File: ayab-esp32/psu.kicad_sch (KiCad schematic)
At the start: 48 parts, among them J602 940, J603 910.930.950.CK35, Q601 BCM857BV, Q602 AO3401A, U401 XL1509, U402 XL1509

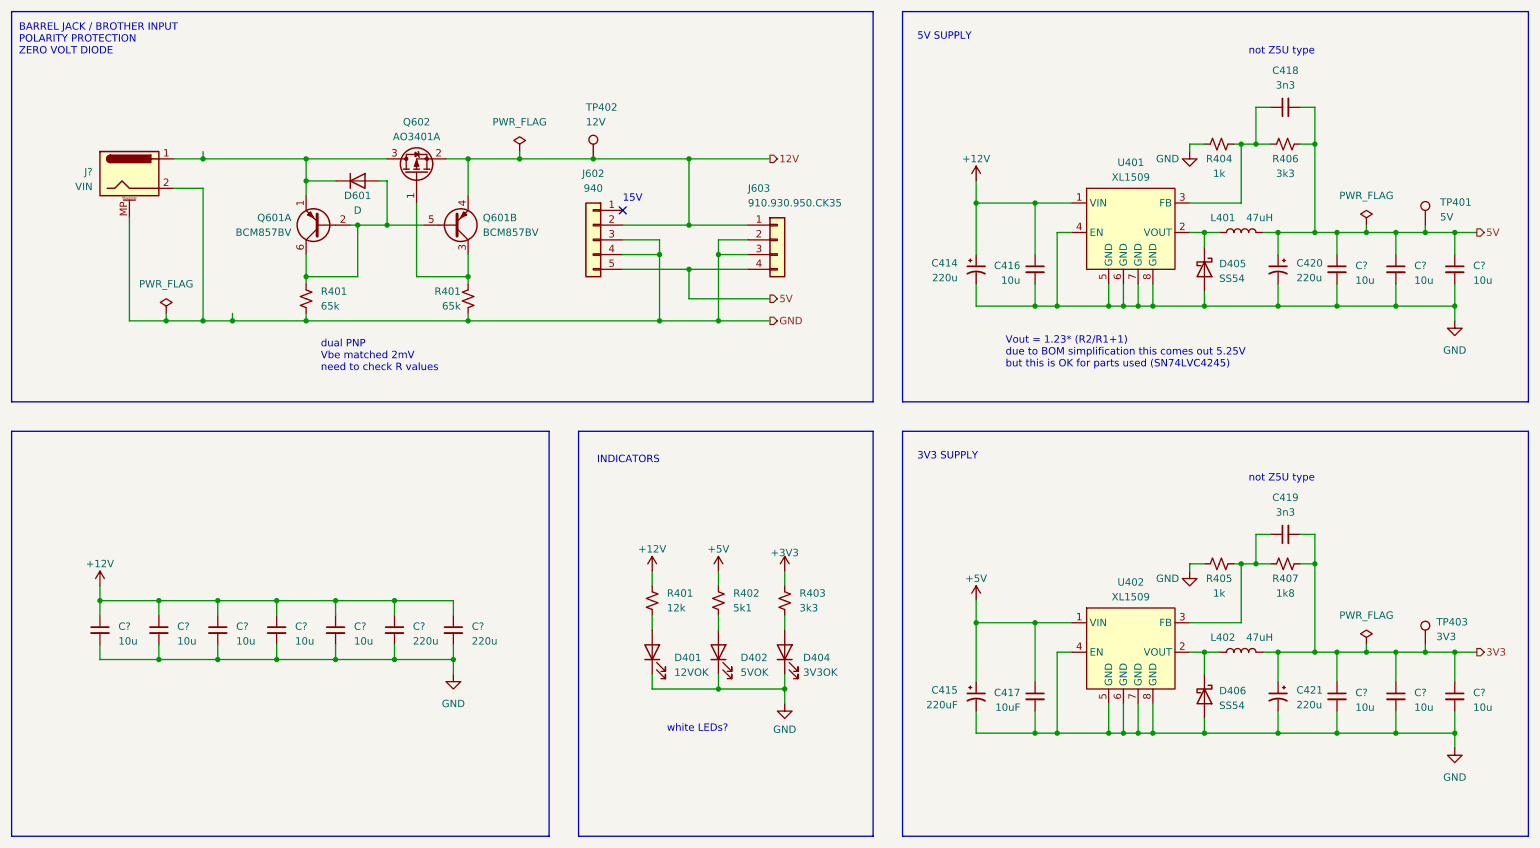
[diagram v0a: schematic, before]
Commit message: add component selection, bom
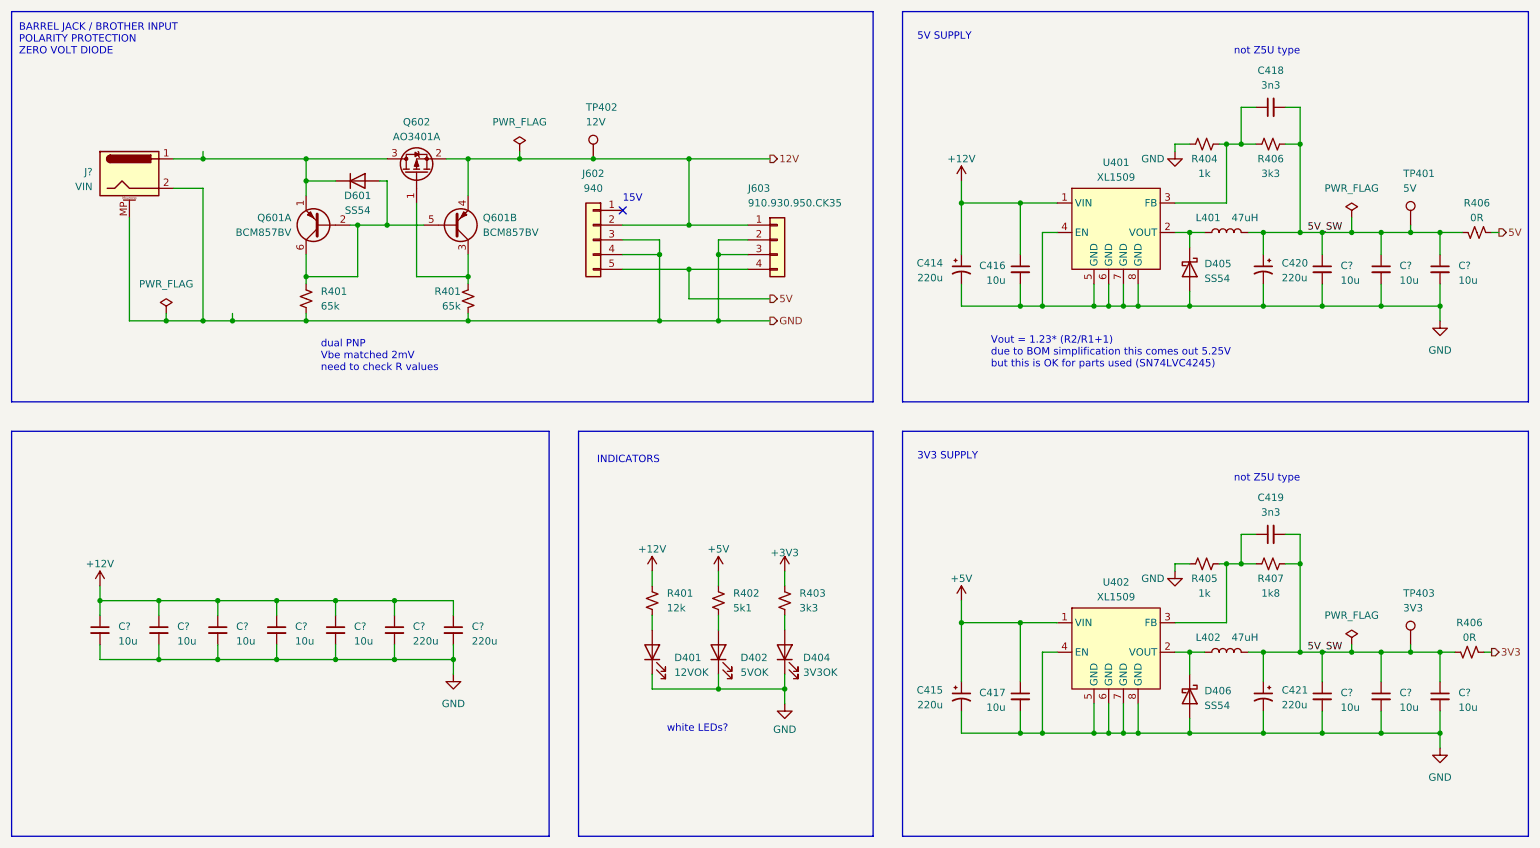
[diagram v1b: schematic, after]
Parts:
- added R406 (x2): 0R, Resistor_SMD:R_0603_1608Metric, symbol Library:R_Small_US
- C414, C420, C421: footprint Capacitor_SMD:CP_Elec_8x10.5 -> Capacitor_THT:CP_Radial_D6.3mm_P2.50mm; symbol ayab-esp32:C_Polarized_Small_US -> Library:C_Polarized_Small_US; LCSC ID (none) -> C44587; OEM (none) -> CX(Dongguan Chengxing Elec); OEM PN (none) -> KS107M025E07RR0VH2FP0; Package (none) -> 0603; Voltage rating (none) -> 25V Aluminum Electrolytic
- C415: value 220uF -> 220u; footprint Capacitor_SMD:CP_Elec_8x10.5 -> Capacitor_THT:CP_Radial_D6.3mm_P2.50mm; symbol ayab-esp32:C_Polarized_Small_US -> Library:C_Polarized_Small_US; LCSC ID (none) -> C44587; OEM (none) -> CX(Dongguan Chengxing Elec); OEM PN (none) -> KS107M025E07RR0VH2FP0; Package (none) -> 0603; Voltage rating (none) -> 25V Aluminum Electrolytic
- C416, C? (x11): footprint Capacitor_SMD:C_0603_1608Metric -> Capacitor_SMD:C_0805_2012Metric; symbol ayab-esp32:C_Small -> Library:C_Small; LCSC ID (none) -> C15850; OEM (none) -> Samsung Electro-Mechanics; OEM PN (none) -> CL21A106KAYNNNE; Package (none) -> 0805; Voltage rating (none) -> 24V X5R
- C417: value 10uF -> 10u; footprint Capacitor_SMD:C_0603_1608Metric -> Capacitor_SMD:C_0805_2012Metric; symbol ayab-esp32:C_Small -> Library:C_Small; LCSC ID (none) -> C15850; OEM (none) -> Samsung Electro-Mechanics; OEM PN (none) -> CL21A106KAYNNNE; Package (none) -> 0805; Voltage rating (none) -> 24V X5R
- C418, C419: symbol ayab-esp32:C_Small -> Library:C_Small; LCSC ID (none) -> C1613; OEM (none) -> Samsung Electro-Mechanics; OEM PN (none) -> CL10B332KB8NNNC; Package (none) -> 0603; Voltage rating (none) -> 50V X7R
- C? (x2): footprint Capacitor_SMD:CP_Elec_8x10.5 -> Capacitor_THT:CP_Radial_D6.3mm_P2.50mm; symbol ayab-esp32:C_Small -> Library:C_Small; LCSC ID (none) -> C44587; OEM (none) -> CX(Dongguan Chengxing Elec); OEM PN (none) -> KS107M025E07RR0VH2FP0; Package (none) -> 0603; Voltage rating (none) -> 25V Aluminum Electrolytic
- D401, D402, D404: symbol ayab-esp32:LED -> Library:LED; LCSC ID (none) -> C2290; OEM (none) -> Hubei KENTO Elec; OEM PN (none) -> C2290; Package (none) -> 0603
- D405, D406: symbol ayab-esp32:D_Schottky -> Library:D_Schottky; LCSC ID (none) -> C2290; OEM (none) -> Hubei KENTO Elec; OEM PN (none) -> SS54; Package (none) -> SMA
- D601: value D -> SS54; footprint (none) -> Diode_SMD:D_SMA; symbol ayab-esp32:D -> Library:D; LCSC ID (none) -> C2290; OEM (none) -> Hubei KENTO Elec; OEM PN (none) -> SS54; Package (none) -> SMA
- J602: symbol ayab-esp32:Conn_01x05 -> Library:Conn_01x05
- J603: symbol ayab-esp32:Conn_01x04 -> Library:Conn_01x04
- J?: symbol ayab-esp32:Barrel_Jack_MountingPin -> Library:Barrel_Jack_MountingPin; LCSC ID (none) -> C2880543; OEM (none) -> XKB Connectivity; OEM PN (none) -> DC-005-2.5A-2.0-SMT
- L401, L402: symbol ayab-esp32:L -> Library:L; LCSC ID (none) -> C9906; OEM (none) -> SXN(Shun Xiang Nuo Elec); OEM PN (none) -> SMDRI127-470MT; Package (none) -> 12x12x8
- Q601: footprint (none) -> Package_TO_SOT_SMD:SOT-363_SC-70-6; symbol ayab-esp32:Q_Dual_PNP_PNP_E1B1C2E2B2C1 -> Library:Q_Dual_PNP_PNP_E1B1C2E2B2C1; LCSC ID (none) -> C105887; OEM (none) -> Nexperia; OEM PN (none) -> BCM857BS,115; Package (none) -> SOT-363
- Q602: symbol ayab-esp32:AO3401A -> Library:AO3401A; LCSC ID (none) -> C15127; OEM (none) -> Alpha & Omega Semicon; OEM PN (none) -> AO3401A; Package (none) -> SOT-23
- R401: symbol ayab-esp32:R_Small_US -> Library:R_Small_US; LCSC ID (none) -> check values; Package (none) -> 0603
- R401: symbol ayab-esp32:R_Small_US -> Library:R_Small_US; LCSC ID (none) -> C22790; OEM (none) -> UNI-ROYAL(Uniroyal Elec); OEM PN (none) -> 0603WAF1202T5E; Package (none) -> 0603
- R402: symbol ayab-esp32:R_Small_US -> Library:R_Small_US; LCSC ID (none) -> C23186; OEM (none) -> UNI-ROYAL(Uniroyal Elec); OEM PN (none) -> 0603WAF5101T5E; Package (none) -> 0603
- R403, R406: symbol ayab-esp32:R_Small_US -> Library:R_Small_US; LCSC ID (none) -> C22978; OEM (none) -> UNI-ROYAL(Uniroyal Elec); OEM PN (none) -> 0603WAF3301T5E; Package (none) -> 0603
- R404, R405: symbol ayab-esp32:R_Small_US -> Library:R_Small_US; LCSC ID (none) -> C21190; OEM (none) -> UNI-ROYAL(Uniroyal Elec); OEM PN (none) -> 0603WAF1001T5E; Package (none) -> 0603
- R407: symbol ayab-esp32:R_Small_US -> Library:R_Small_US; LCSC ID (none) -> C4177; OEM (none) -> UNI-ROYAL(Uniroyal Elec); OEM PN (none) -> 0603WAF1801T5E; Package (none) -> 0603
- TP401, TP402, TP403: footprint TestPoint:TestPoint_Pad_D1.0mm -> TestPoint:TestPoint_Pad_D2.0mm; symbol ayab-esp32:TestPoint -> Library:TestPoint; now left out of the parts list
- U401, U402: symbol ayab-esp32:XL1509 -> Library:XL1509; LCSC ID (none) -> C61063; OEM (none) -> XLSEMI; OEM PN (none) -> XL1509-5.0E1; Package (none) -> SOIC-8
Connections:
- net 3V3: now also R406.2; no longer C419.2, C421.1, C?.1, C?.1, C?.1, L402.2, R407.2, TP403.1
- net 5V: now also R406.2; no longer C418.2, C420.1, C?.1, C?.1, C?.1, L401.2, R406.2, TP401.1
- new net 5V_SW: C418.2, C419.2, C420.1, C421.1, C?.1, C?.1, C?.1, C?.1, C?.1, C?.1, L401.2, L402.2, R406.1, R406.1, R406.2, R407.2, TP401.1, TP403.1
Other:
- moved on the sheet: C414, C415, C416, C417, C418, C419, C420, C421, C?, D405, D406, L401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

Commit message: review ZVD P-ch MOSFET and resistors
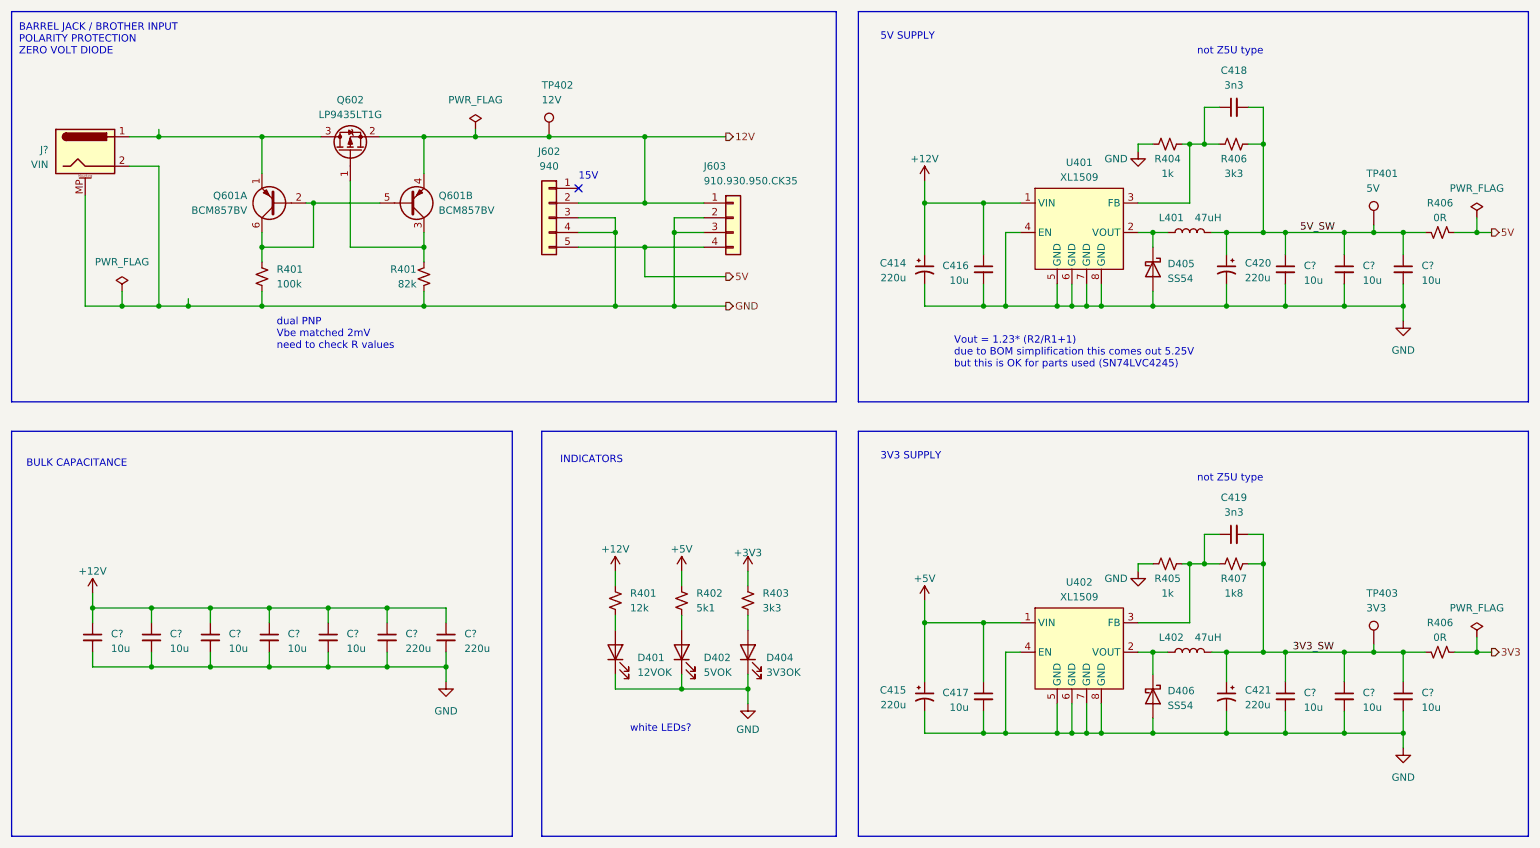
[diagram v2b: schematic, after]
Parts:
- removed D601: SS54, Diode_SMD:D_SMA, symbol Library:D
- C414, C415, C420, C421: symbol Library:C_Polarized_Small_US -> ayab-lib:C_Polarized_Small_US
- C416, C417, C418, C419, C? (x13): symbol Library:C_Small -> ayab-lib:C_Small
- D401, D402, D404: symbol Library:LED -> ayab-lib:LED
- D405, D406: symbol Library:D_Schottky -> ayab-lib:D_Schottky
- J602: symbol Library:Conn_01x05 -> ayab-lib:Conn_01x05
- J603: symbol Library:Conn_01x04 -> ayab-lib:Conn_01x04
- J?: symbol Library:Barrel_Jack_MountingPin -> ayab-lib:Barrel_Jack_MountingPin
- L401, L402: symbol Library:L -> ayab-lib:L
- Q601: symbol Library:Q_Dual_PNP_PNP_E1B1C2E2B2C1 -> ayab-lib:Q_Dual_PNP_PNP_E1B1C2E2B2C1
- Q602: value AO3401A -> LP9435LT1G; symbol Library:AO3401A -> ayab-lib:AO3401A; LCSC ID C15127 -> C383257; OEM Alpha & Omega Semicon -> LRC; OEM PN AO3401A -> LP9435LT1G; Voltage rating (none) -> 30V
- R401: value 65k -> 82k; symbol Library:R_Small_US -> ayab-lib:R_Small_US; LCSC ID check values -> C23254; OEM (none) -> UNI-ROYAL(Uniroyal Elec); OEM PN (none) -> 0603WAF8202T5E
- R401, R402, R403, R404, R405, R406, R407: symbol Library:R_Small_US -> ayab-lib:R_Small_US
- R401: value 65k -> 100k; symbol Library:R_Small_US -> ayab-lib:R_Small_US; LCSC ID check values -> C25803; OEM (none) -> UNI-ROYAL(Uniroyal Elec); OEM PN (none) -> 0603WAF1003T5E
- TP401, TP402, TP403: symbol Library:TestPoint -> ayab-lib:TestPoint
- U401, U402: symbol Library:XL1509 -> ayab-lib:XL1509
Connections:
- net 5V_SW: no longer C419.2, C421.1, C?.1, C?.1, C?.1, L402.2, R406.1, R407.2, TP403.1
- new net 3V3_SW: C419.2, C421.1, C?.1, C?.1, C?.1, L402.2, R406.1, R407.2, TP403.1
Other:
- note added: "BULK CAPACITANCE"
- moved on the sheet: C414, C415, C416, C417, C418, C419, C420, C421, C?, D401, D402, D404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

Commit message: first draft layout DRC clean
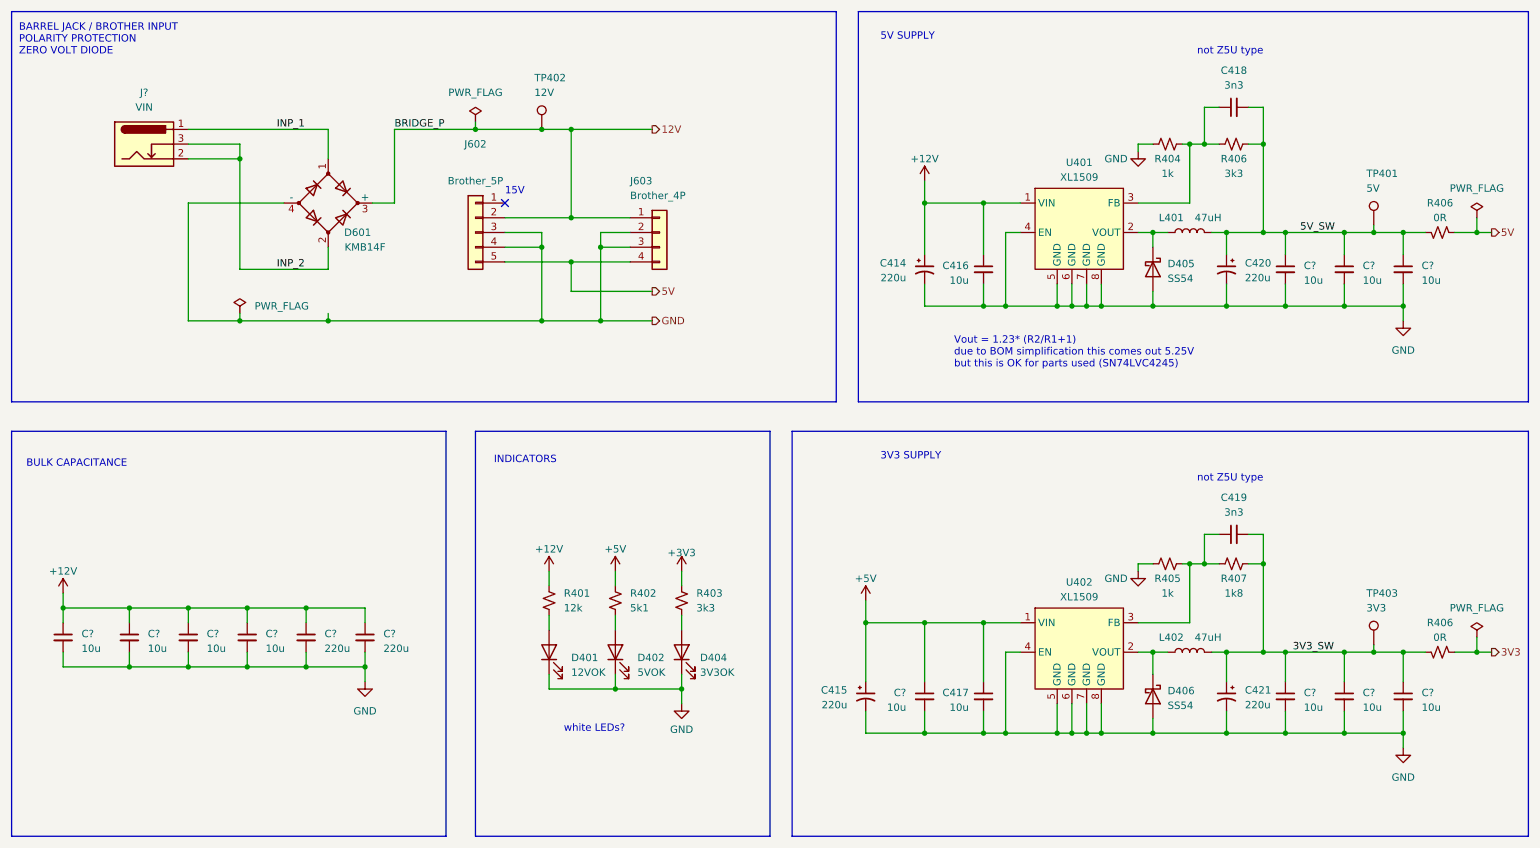
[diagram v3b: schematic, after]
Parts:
- removed Q601: BCM857BV, Package_TO_SOT_SMD:SOT-363_SC-70-6, symbol ayab-lib:Q_Dual_PNP_PNP_E1B1C2E2B2C1
- removed Q602: LP9435LT1G, Package_TO_SOT_SMD:SOT-23, symbol ayab-lib:AO3401A
- removed R401: 82k, Resistor_SMD:R_0603_1608Metric, symbol ayab-lib:R_Small_US
- removed R401: 100k, Resistor_SMD:R_0603_1608Metric, symbol ayab-lib:R_Small_US
- added D601: KMB14F, easyeda2kicad:MBF-SMD_L4.8-W3.8-P2.54-LS6.8-TL, symbol Device:D_Bridge_+-AA
- J602: value 940 -> Brother_5P; footprint (none) -> Library:Brother_5P; now left out of the parts list
- J603: value 910.930.950.CK35 -> Brother_4P; footprint (none) -> Library:Brother_4P; now left out of the parts list
- J?: symbol ayab-lib:Barrel_Jack_MountingPin -> Connector:Barrel_Jack_Switch
- TP401, TP402, TP403: footprint TestPoint:TestPoint_Pad_D2.0mm -> TestPoint:TestPoint_Pad_D1.0mm
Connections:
- net +12V: no longer C?.1
- net +5V: now also C?.1
- net 12V: now also D601.3 (+)
- net GND: now also D601.4 (-); no longer J?.2, J?.MP (MountPin)
- net INP_1: now reaches J?.1
- net INP_1: now also D601.1
- new net INP_2: D601.2, J?.2, J?.3
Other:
- note removed: "dual PNP Vbe matched 2mV need to check R values"
- moved on the sheet: C415, C?, D401, D402, D404, J602, J603, J?, R401, R402, R403, TP402

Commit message: revise connector positions
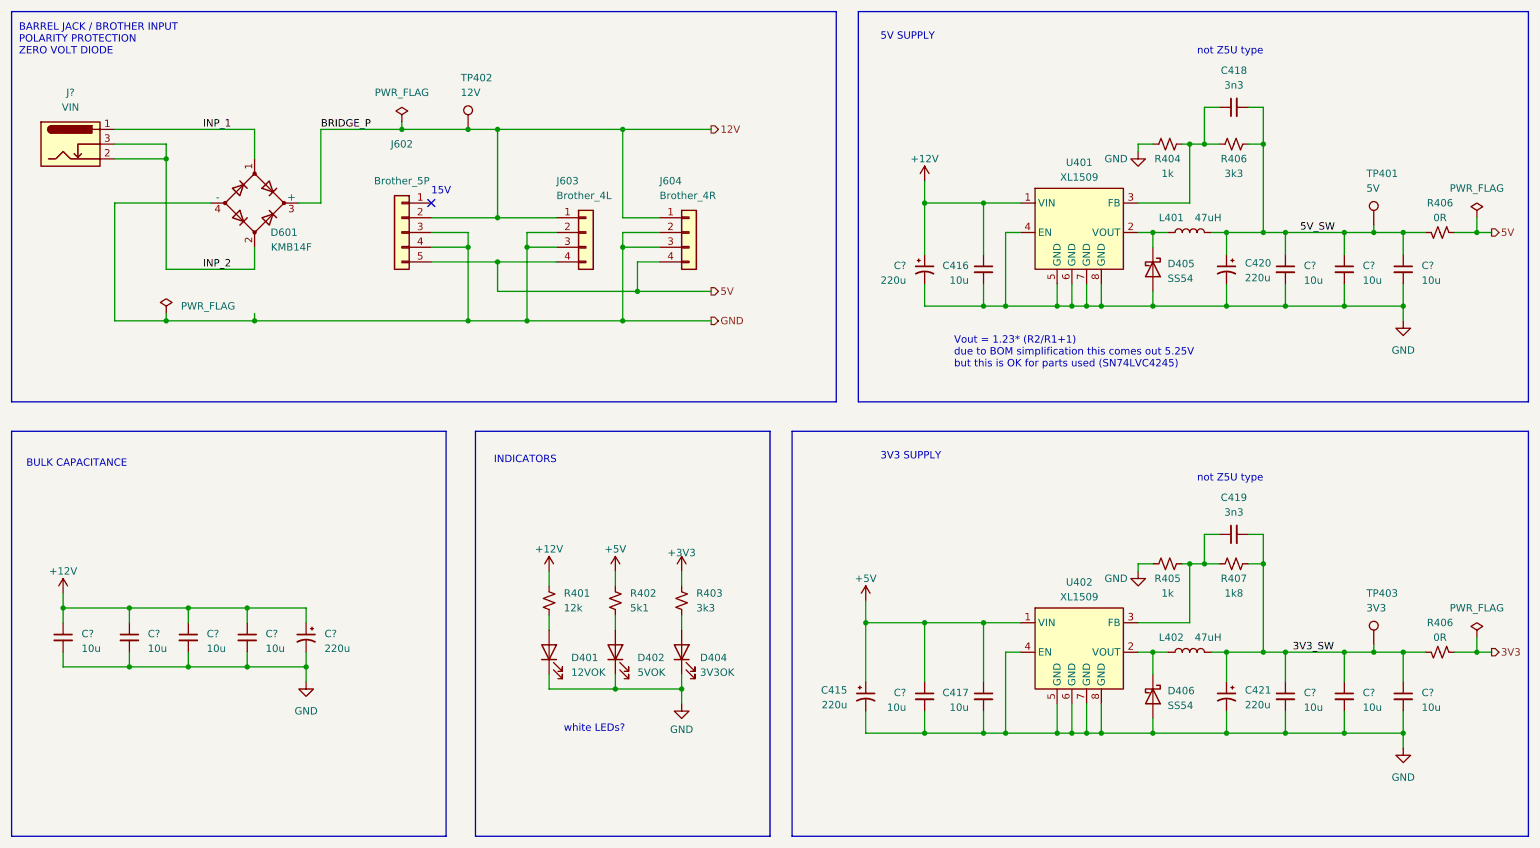
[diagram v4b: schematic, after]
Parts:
- removed C414: 220u, Capacitor_THT:CP_Radial_D6.3mm_P2.50mm, symbol ayab-lib:C_Polarized_Small_US
- added J604: Brother_4R, Library:Brother_4P, symbol ayab-lib:Conn_01x04
- C? (x2): symbol ayab-lib:C_Small -> ayab-lib:C_Polarized_Small_US
- D601: LCSC ID (none) -> C880909; OEM (none) -> FUXINSEMI; OEM PN (none) -> KMB14F
- J603: value Brother_4P -> Brother_4L
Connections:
- net 12V: now also J604.1 (Pin_1)
- net 5V: now also J604.4 (Pin_4)
- net GND: now also J604.2 (Pin_2), J604.3 (Pin_3)
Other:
- moved on the sheet: D601, J602, J603, J?, TP402

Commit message: production files
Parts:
- removed J603: Brother_4L, Library:Brother_4P, symbol ayab-lib:Conn_01x04
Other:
- moved on the sheet: J604
